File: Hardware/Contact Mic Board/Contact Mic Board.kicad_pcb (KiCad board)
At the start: 4 copper layers, 31 x 18 mm, 47 parts, among them J1 Conn_01x09_Pin, U1 ES8388, U2 MCP6002-xMC

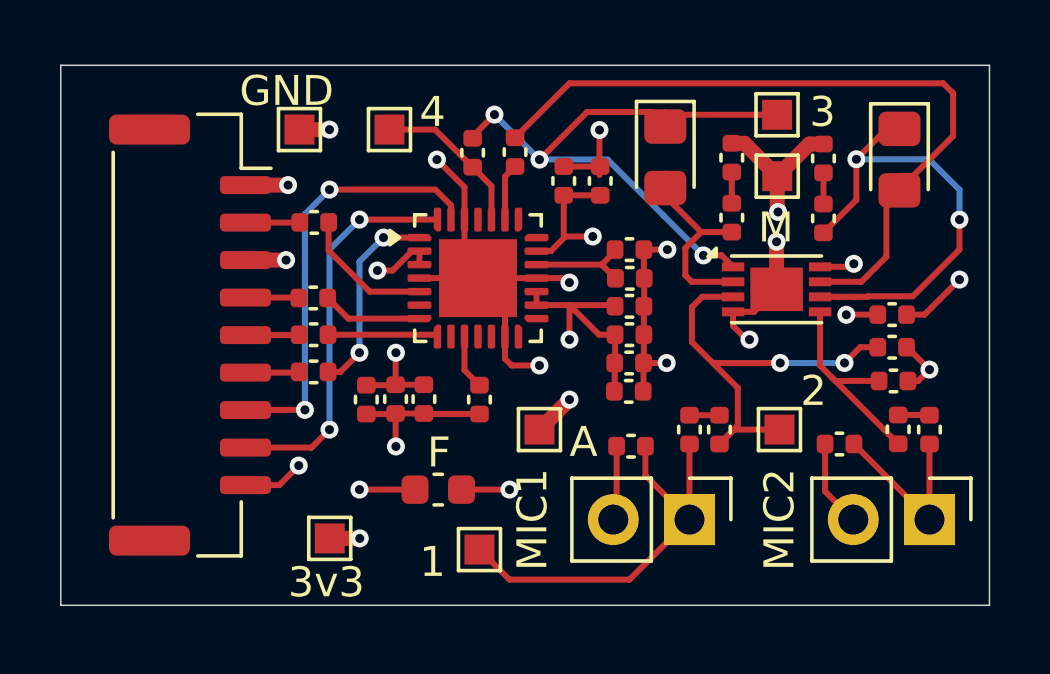
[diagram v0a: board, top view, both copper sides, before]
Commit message: received feedback from Andy + others and revised board
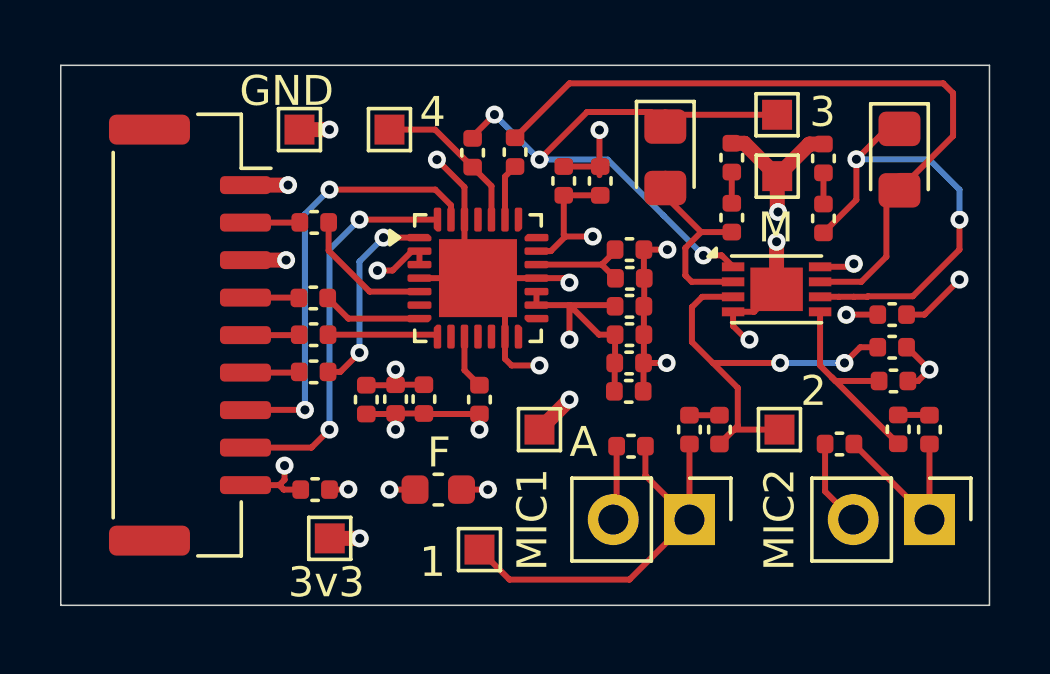
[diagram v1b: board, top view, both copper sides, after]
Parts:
- added C20: 10uF, Capacitor_SMD:C_0402_1005Metric, F.Cu at (111.5, 62.0)
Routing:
- net +3.3V: track 10.0 -> 9.03 mm
- net +3.3VA: track 13.3 -> 12.6 mm
- net GND: track 43.8 -> 44.4 mm, vias 13 -> 15
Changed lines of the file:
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@@
 		)
 	)
+	(footprint "Capacitor_SMD:C_0402_1005Metric"
+		(layer "F.Cu")
+		(at 111.52 62)
+		(descr "Capacitor SMD 0402 (1005 Metric), square (rectangular) end terminal, IPC-7351 nominal, (Body size source: IPC-SM-782 page 76, https://www.pcb-3d.com/wordpress/wp-content/uploads/ipc-sm-782a_amendment_1_and_2.pdf), generated with kicad-footprint-generator")
+		(tags "capacitor")
+		(property "Reference" "C20"
+			(at 0 -1.16 0)
+			(layer "F.SilkS")
+			(hide yes)
+			(effects
+				(font
+					(size 1 1)
+					(thickness 0.15)
+				)
+			)
+		)
+		(property "Value" "10uF"
+			(at 0 1.16 0)
+			(layer "F.Fab")
+			(hide yes)
+			(effects
+				(font
+					(size 1 1)
+					(thickness 0.15)
+				)
+			)
+		)
+		(property "Datasheet" "~"
+			(at 0 0 0)
+			(layer "F.Fab")
+			(hide yes)
+			(effects
+				(font
+					(size 1.27 1.27)
+					(thickness 0.15)
+				)
+			)
+		)
+		(property "Description" "Polarized capacitor, small US symbol"
+			(at 0 0 0)
+			(layer "F.Fab")
+			(hide yes)
+			(effects
+				(font
+					(size 1.27 1.27)
+					(thickness 0.15)
+				)
+			)
+		)
+		(property ki_fp_filters "CP_*")
+		(sheetname "/")
+		(sheetfile "Contact Mic Board.kicad_sch")
+		(attr smd)
+		(fp_line
+			(start -0.107836 -0.36)
+			(end 0.107836 -0.36)
+			(stroke
+				(width 0.12)
+				(type solid)
+			)
+			(layer "F.SilkS")
+		)
+		(fp_line
+			(start -0.107836 0.36)
+			(end 0.107836 0.36)
+			(stroke
+				(width 0.12)
+				(type solid)
+			)
+			(layer "F.SilkS")
+		)
+		(fp_rect
+			(start -0.91 -0.46)
+			(end 0.91 0.46)
+			(stroke
+				(width 0.05)
+				(type solid)
+			)
+			(fill no)
+			(layer "F.CrtYd")
+		)
+		(fp_rect
+			(start -0.5 -0.25)
+			(end 0.5 0.25)
+			(stroke
+				(width 0.1)
+				(type solid)
+			)
+			(fill no)
+			(layer "F.Fab")
+		)
+		(fp_text user "${REFERENCE}"
+			(at 0 0 0)
+			(layer "F.Fab")
+			(effects
+				(font
+					(size 0.25 0.25)
+					(thickness 0.04)
+				)
+			)
+		)
+		(pad "1" smd roundrect
+			(at -0.48 0)
+			(size 0.56 0.62)
+			(layers "F.Cu" "F.Mask" "F.Paste")
+			(roundrect_rratio 0.25)
+			(net 1 "+3.3V")
+			(pintype "passive")
+		)
+		(pad "2" smd roundrect
+			(at 0.48 0)
+			(size 0.56 0.62)
+			(layers "F.Cu" "F.Mask" "F.Paste")
+			(roundrect_rratio 0.25)
+			(net 2 "GND")
+			(pintype "passive")
+		)
+		(embedded_fonts no)
+		(model "${KICAD9_3DMODEL_DIR}/Capacitor_SMD.3dshapes/C_0402_1005Metric.step"
+			(offset
+				(xyz 0 0 0)
+			)
+			(scale
+				(xyz 1 1 1)
+			)
+			(rotate
+				(xyz 0 0 0)
+			)
+		)
+	)
 	(footprint "Package_DFN_QFN:DFN-8-1EP_3x2mm_P0.5mm_EP1.75x1.45mm"
 		(layer "F.Cu")
@@
 	)
 	(segment
-		(start 114.203108 57.64054)
-		(end 114.203108 58.503202)
+		(start 113.6 54.697082)
+		(end 114.102918 54.697082)
 		(width 0.2)
 		(layer "F.Cu")
@@
 	)
 	(segment
-		(start 113.6 54.697082)
-		(end 114.102918 54.697082)
+		(start 115 54.05)
+		(end 115 54.5)
 		(width 0.2)
 		(layer "F.Cu")
@@
 	)
 	(segment
-		(start 115 54.05)
-		(end 115 54.5)
+		(start 110.325735 61.85)
+		(end 109.2 61.85)
 		(width 0.2)
 		(layer "F.Cu")
@@
 	)
 	(segment
-		(start 114.18631 58.52)
+		(start 114.203108 58)
 		(end 114.203108 58.503202)
 		(width 0.2)
@@
 	)
 	(segment
-		(start 114.214477 57.629171)
-		(end 114.203108 57.64054)
+		(start 114.18631 58.52)
+		(end 114.203108 58.503202)
 		(width 0.2)
 		(layer "F.Cu")
@@
 	)
 	(segment
-		(start 114.851624 62)
-		(end 113 62)
+		(start 111.04 62)
+		(end 110.475735 62)
 		(width 0.2)
 		(layer "F.Cu")
@@
 	)
 	(segment
-		(start 110.325735 61.85)
-		(end 110.975735 61.2)
+		(start 110.475735 62)
+		(end 110.325735 61.85)
 		(width 0.2)
 		(layer "F.Cu")
@@
 	)
 	(segment
-		(start 112.009121 63.62603)
-		(end 113.009121 63.62603)
-		(width 0.5)
+		(start 114.851624 62)
+		(end 114 62)
+		(width 0.2)
 		(layer "F.Cu")
 		(net 1)
 	)
 	(segment
-		(start 109.2 61.85)
-		(end 110.325735 61.85)
+		(start 110.502712 61.2)
+		(end 110.502712 61.673023)
 		(width 0.2)
 		(layer "F.Cu")
@@
 	)
 	(segment
-		(start 114.214477 57.437432)
-		(end 114.214477 57.629171)
+		(start 112.009121 63.62603)
+		(end 113.009121 63.62603)
+		(width 0.5)
+		(layer "F.Cu")
+		(net 1)
+	)
+	(segment
+		(start 110.502712 61.673023)
+		(end 110.325735 61.85)
 		(width 0.2)
 		(layer "F.Cu")
@@
 	)
 	(via
-		(at 110.975735 61.2)
+		(at 110.502712 61.2)
 		(size 0.6)
 		(drill 0.3)
@@
 	)
 	(via
-		(at 114.214477 57.437432)
+		(at 114.203108 58)
 		(size 0.6)
 		(drill 0.3)
@@
 	)
 	(via
-		(at 113 62)
+		(at 114 62)
 		(size 0.6)
 		(drill 0.3)
@@
 	)
 	(segment
+		(start 112.620485 62)
+		(end 112.630383 61.990102)
+		(width 0.2)
+		(layer "F.Cu")
+		(net 2)
+	)
+	(segment
 		(start 122.48 57.768132)
 		(end 122.468038 57.780094)
@@
 	)
 	(segment
-		(start 114.203108 60.550267)
-		(end 114.21507 60.562229)
+		(start 119 57.862674)
+		(end 118.072591 57.862674)
 		(width 0.2)
 		(layer "F.Cu")
@@
 	)
 	(segment
-		(start 119 57.862674)
-		(end 118.072591 57.862674)
+		(start 112 62)
+		(end 112.620485 62)
 		(width 0.2)
 		(layer "F.Cu")
@@
 	)
 	(segment
+		(start 114.203108 60)
+		(end 114.203108 59.463202)
+		(width 0.2)
+		(layer "F.Cu")
+		(net 2)
+	)
+	(segment
 		(start 117.85 55.85)
 		(end 117.85 56.9)
@@
 	)
 	(segment
+		(start 117 59.48)
+		(end 117 60)
+		(width 0.2)
+		(layer "F.Cu")
+		(net 2)
+	)
+	(segment
 		(start 121.023563 51.230361)
 		(end 121.024923 51.231721)
@@
 		(net 2)
 	)
-	(segment
-		(start 114.203108 59.463202)
-		(end 114.203108 60.550267)
-		(width 0.2)
-		(layer "F.Cu")
-		(net 2)
-	)
 	(via
 		(at 126 57)
@@
 	)
 	(via
-		(at 114.21507 60.562229)
+		(at 114.203108 60)
 		(size 0.6)
 		(drill 0.3)
@@
 	)
 	(via
+		(at 112.630383 61.990102)
+		(size 0.6)
+		(drill 0.3)
+		(layers "F.Cu" "B.Cu")
+		(net 2)
+	)
+	(via
 		(at 123.240754 57.780094)
 		(size 0.6)
@@
 		(net 2)
 	)
+	(via
+		(at 117 60)
+		(size 0.6)
+		(drill 0.3)
+		(layers "F.Cu" "B.Cu")
+		(net 2)
+	)
+	(segment
+		(start 116.401624 62)
+		(end 117.280128 62)
+		(width 0.2)
+		(layer "F.Cu")
+		(net 3)
+	)
 	(segment
 		(start 119 60)
@@
 	)
 	(segment
-		(start 116.401624 62)
-		(end 118 62)
-		(width 0.2)
-		(layer "F.Cu")
-		(net 3)
-	)
-	(segment
 		(start 120 55.85)
 		(end 121.479953 55.85)
@@
 	)
 	(via
-		(at 118 62)
+		(at 117.280128 62)
 		(size 0.6)
 		(drill 0.3)

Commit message: submitted for manufacturinng. Flipped contact mic connections on main board to be aligned with contact mic board
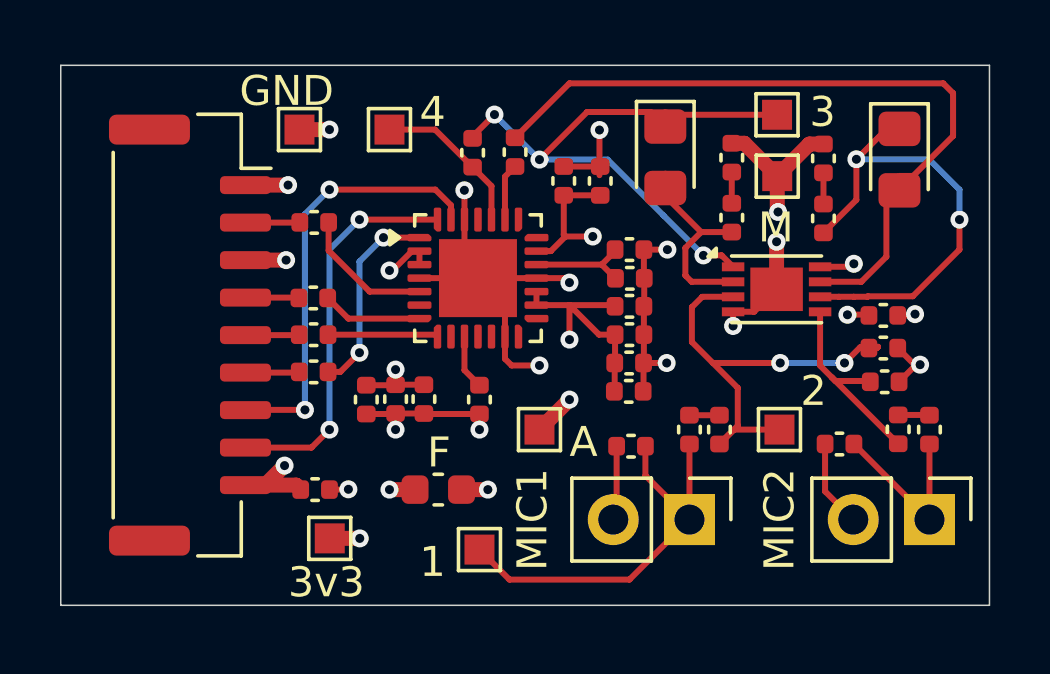
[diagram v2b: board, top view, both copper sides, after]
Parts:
- moved R3 0.30 mm to (130.5, 57.3)
- moved R4 0.30 mm to (130.5, 58.4)
- moved C19 0.30 mm to (130.5, 56.2)
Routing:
- net GND: track 44.4 -> 40.6 mm

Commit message: fixed power button and via proximity to pad on main board
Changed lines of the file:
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@@
+	)
+	(segment
+		(start 131.519118 56.151346)
+		(end 131.476713 56.193751)
+		(width 0.2)
+		(layer "F.Cu")
+		(net 2)
 	)
 	(segment
@@
 		(start 122.491962 55.878085)
 		(end 122.48 55.890047)
+		(width 0.2)
+		(layer "F.Cu")
+		(net 2)
+	)
+	(segment
+		(start 131.476713 56.193751)
+		(end 130.941764 56.193751)
 		(width 0.2)
 		(layer "F.Cu")
@@
 	)
 	(segment
-		(start 130.941764 56.193751)
-		(end 131.476713 56.193751)
-		(width 0.2)
-		(layer "F.Cu")
-		(net 2)
-	)
-	(segment
 		(start 114.18631 59.48)
 		(end 114.203108 59.463202)
@@
 		(width 0.2)
 		(layer "F.Cu")
-		(net 2)
-	)
-	(segment
-		(start 131.476713 56.193751)
-		(end 131.519118 56.151346)
-		(width 0.2)
-		(layer "F.Cu")
